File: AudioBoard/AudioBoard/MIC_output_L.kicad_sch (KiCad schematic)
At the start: 0 parts

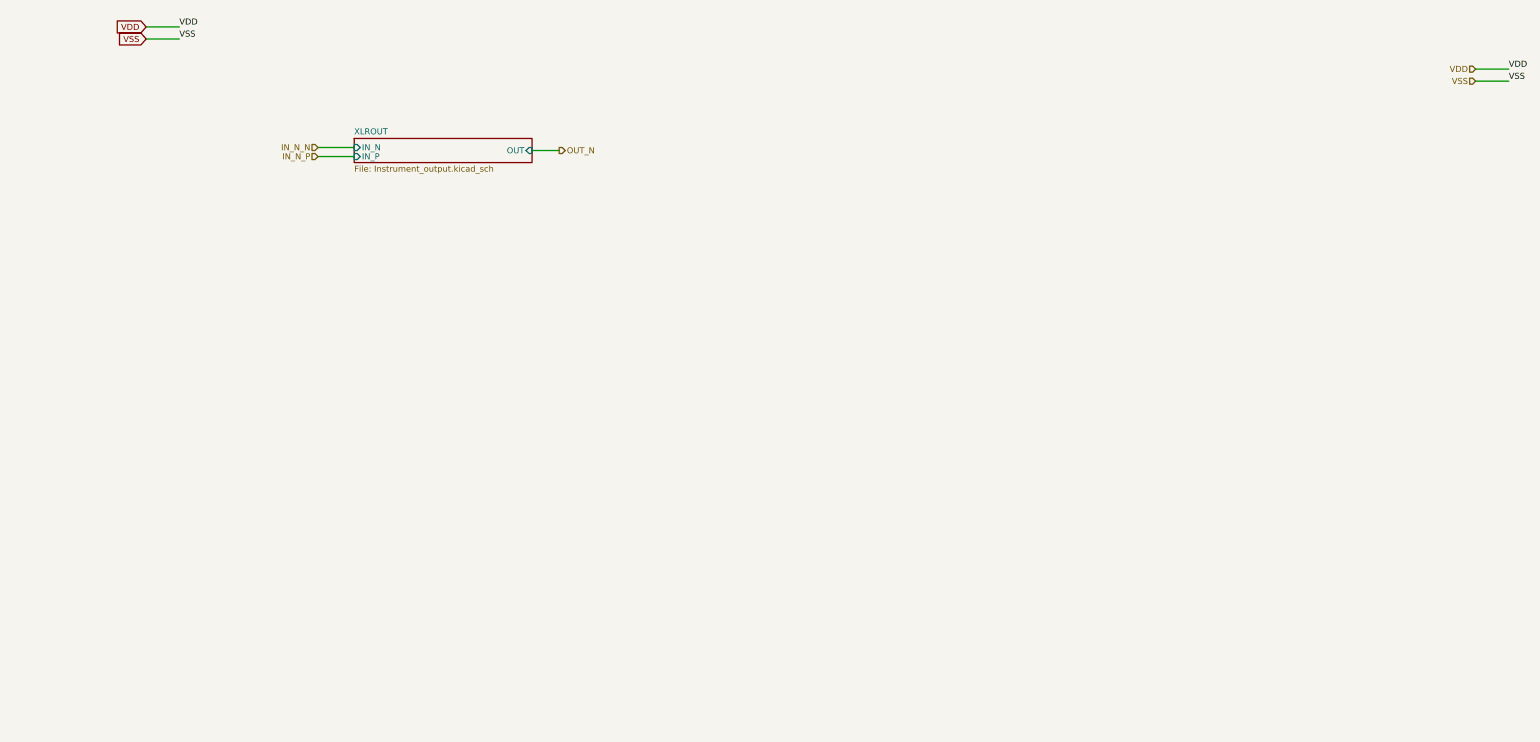
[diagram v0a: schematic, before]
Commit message: added first time routing to see crosssections
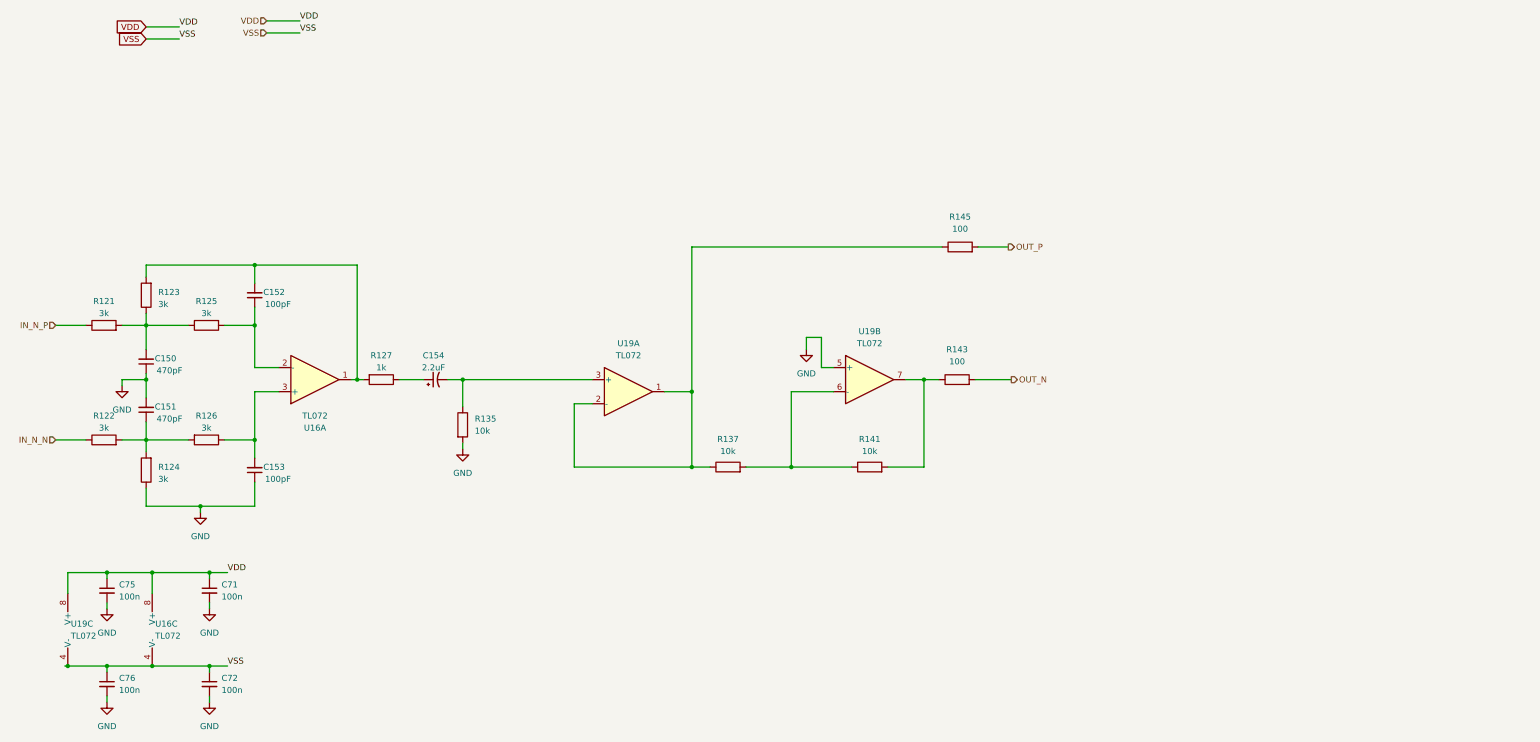
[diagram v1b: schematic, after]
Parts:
- added C150, C151: 470pF, Capacitor_SMD:C_0603_1608Metric, symbol Device:C_Small
- added C152, C153: 100pF, Capacitor_SMD:C_0603_1608Metric, symbol Device:C_Small
- added C154: 2.2uF, Capacitor_SMD:C_0805_2012Metric_Pad1.18x1.45mm_HandSolder, symbol Device:C_Polarized_Small_US
- added C71, C72, C75, C76: 100n, Capacitor_SMD:C_0402_1005Metric, symbol Device:C_Small
- added R121, R122, R123, R124, R125, R126: 3k, Resistor_SMD:R_0603_1608Metric, symbol Device:R
- added R127: 1k, Resistor_SMD:R_0603_1608Metric, symbol Device:R
- added R135, R137, R141: 10k, Resistor_SMD:R_0603_1608Metric, symbol Device:R
- added R143, R145: 100, Resistor_SMD:R_0603_1608Metric, symbol Device:R
- added U16, U19: TL072, Package_SO:SOIC-8_3.9x4.9mm_P1.27mm, symbol Amplifier_Operational:TL072
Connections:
- net IN_N_N: now also R122.1
- net IN_N_P: now also R121.1
- net OUT_N: now also R143.2
- net VDD: now also C71.1, C75.1, U16.8 (V+), U19.8 (V+)
- net VSS: now also C72.1, C76.1, U16.4 (V-), U19.4 (V-)
- new net: C154.2, R135.1, U19.3 (+)
- new net: R141.2, R143.1, U19.7
- new net: C153.2, R126.1, U16.3 (+)
- new net: C151.1, R122.2, R124.2, R126.2
- new net: R137.2, R141.1, U19.6 (-)
- new net: R137.1, R145.1, U19.1, U19.2 (-)
- new net: C154.1, R127.1
- new net: C150.2, R121.2, R123.1, R125.1
- new net: C152.2, R123.2, R127.2, U16.1
- new net: C152.1, R125.2, U16.2 (-)
- new net GND: C150.1, C151.2, C153.1, C71.2, C72.2, C75.2, C76.2, R124.1, R135.2, U19.5 (+)
- new net OUT_P: R145.2
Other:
- removed sheet XLROUT

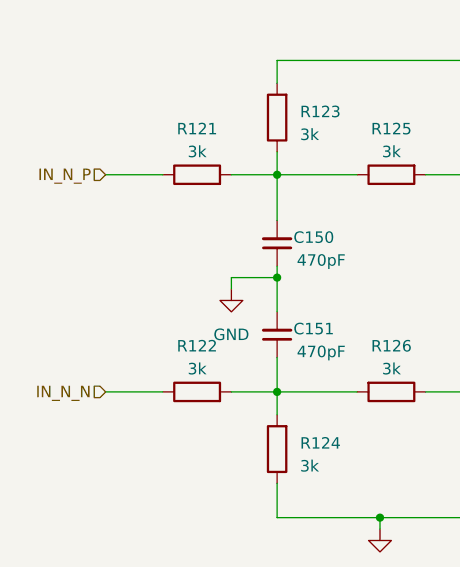
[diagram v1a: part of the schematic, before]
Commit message: optimized codec layout
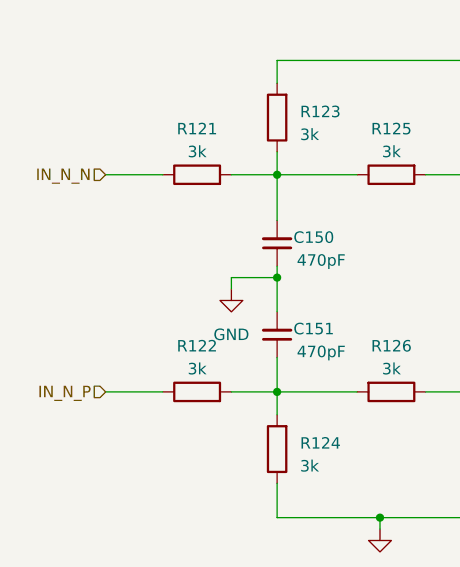
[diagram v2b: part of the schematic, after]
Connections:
- net IN_N_N: now also R121.1; no longer R122.1
- net IN_N_P: now also R122.1; no longer R121.1
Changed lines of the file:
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@@
 	(hierarchical_label "IN_N_P"
+		(shape input)
+		(at 29.845 114.3 180)
+		(effects
+			(font
+				(size 1.27 1.27)
+			)
+			(justify right)
+		)
+	)
+	(hierarchical_label "IN_N_N"
 		(shape input)
 		(at 29.845 90.17 180)
@@
 		)
 	)
-	(hierarchical_label "IN_N_N"
-		(shape input)
-		(at 29.845 114.3 180)
-		(effects
-			(font
-				(size 1.27 1.27)
-			)
-			(justify right)
-		)
-	)

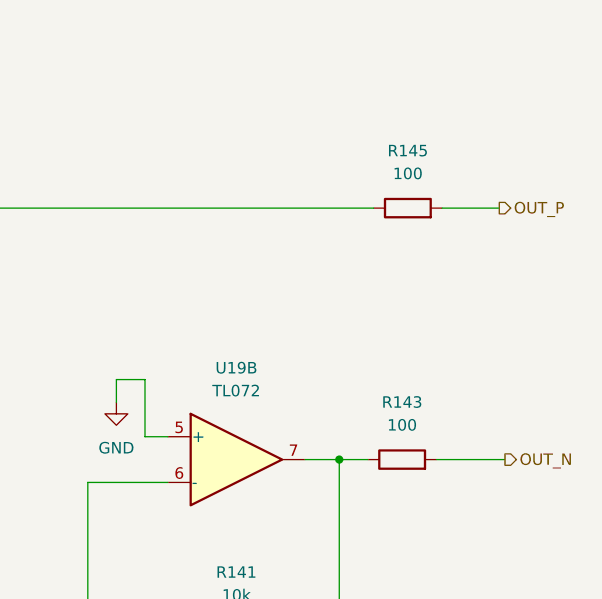
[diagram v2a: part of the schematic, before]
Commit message: assigned footprint to elements lcsc parts
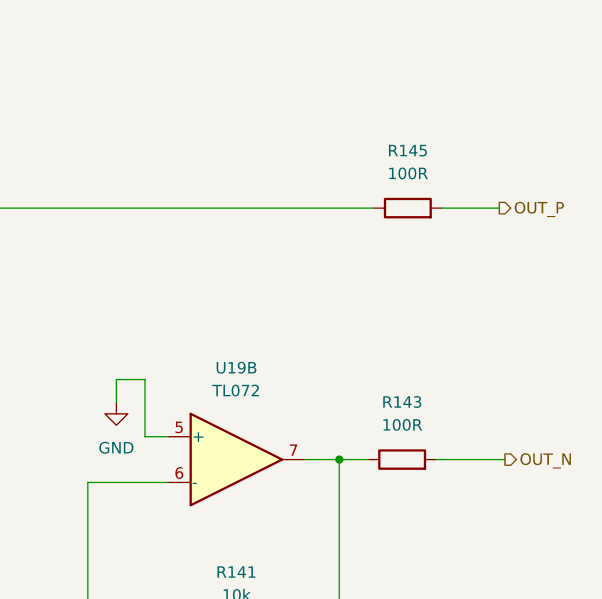
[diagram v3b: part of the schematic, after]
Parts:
- R135, R137, R141: JLCPCB (none) -> C4184; LCSC Part (none) -> C4184
- R143, R145: value 100 -> 100R; footprint Resistor_SMD:R_0603_1608Metric -> Resistor_SMD:R_0402_1005Metric; JLCPCB (none) -> C25076; LCSC Part (none) -> C25076
